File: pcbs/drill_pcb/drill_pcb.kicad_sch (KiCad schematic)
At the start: 78 parts, among them SW1 RPi reset, SW2 SW_Push, SW3 SW_Push, SW4 SW_Push, U1 PCA9306, U2 Pico, U3 L7805, U4 IFX007T, U5 IFX007T, U6 ACS712xLCTR-20A, U7 HT75xx-1-SOT89

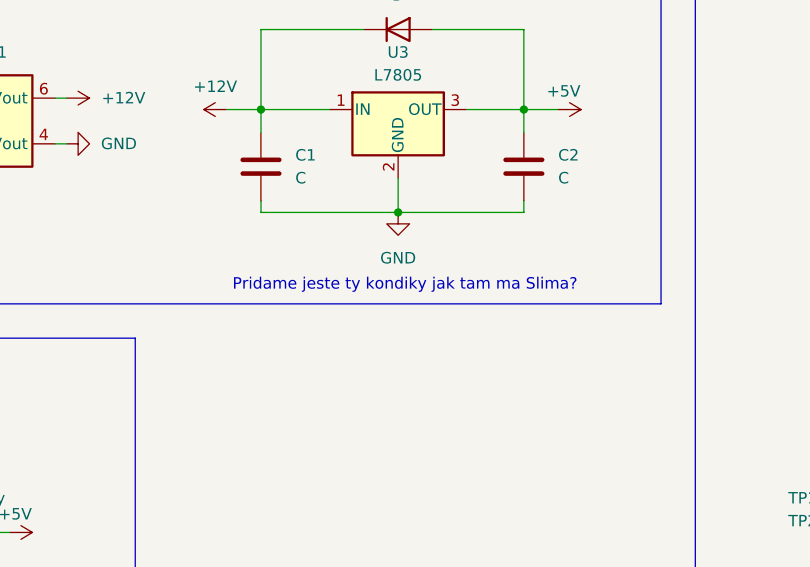
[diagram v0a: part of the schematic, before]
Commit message: delete comments
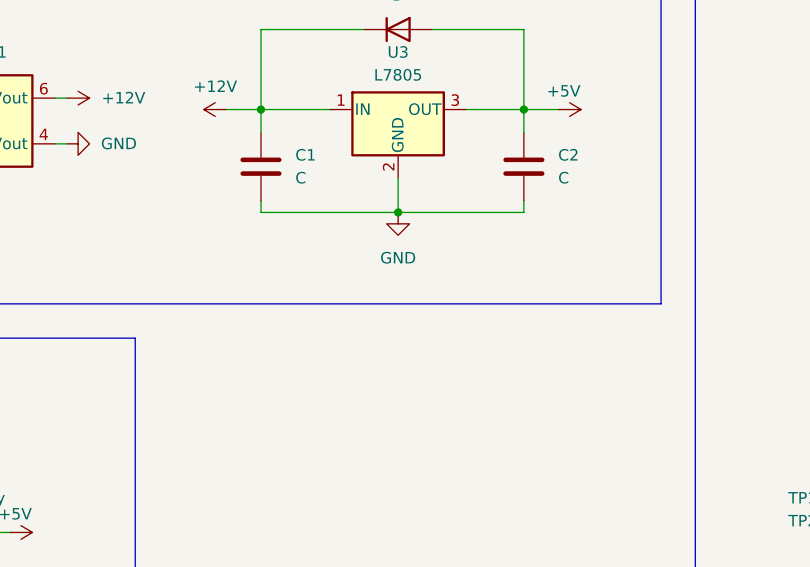
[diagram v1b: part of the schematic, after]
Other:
- note removed: "Pridame jeste ty kondiky jak tam ma Slima?"
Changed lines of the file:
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@@
-		)
-	)
-	(text "Pridame jeste ty kondiky jak tam ma Slima?"
-		(exclude_from_sim no)
-		(at 153.162 51.308 0)
-		(effects
-			(font
-				(size 1.27 1.27)
-			)
 		)
 	)

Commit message: pridany_pojezd
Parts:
- added A4: Arduino_Nano_v3.x, Module:Arduino_Nano, symbol MCU_Module:Arduino_Nano_v3.x
- added A5, A6: Driver_TMC2209, Module:Pololu_Breakout-16_15.2x20.3mm, symbol mujDriver:mujDriver2
- added C18, C21: 4μ7, Capacitor_THT:CP_Radial_D5.0mm_P2.50mm, symbol Device:C_Polarized
- added C19, C20: 100 nF, Capacitor_THT:C_Disc_D4.3mm_W1.9mm_P5.00mm, symbol Device:C
- added C22, C23: 100μ, Capacitor_THT:CP_Radial_D8.0mm_P3.50mm, symbol Device:C_Polarized
- added J1: 12V, Connector_AMASS:AMASS_XT60-M_1x02_P7.20mm_Vertical, symbol Connector:Screw_Terminal_01x02
- added J10: TOF_senzor, Connector_JST:JST_XH_B3B-XH-A_1x03_P2.50mm_Vertical, symbol Connector:Screw_Terminal_01x03
- added J11, J12, J5, J6: Screw_Terminal_01x03, Connector_JST:JST_XH_S3B-XH-A-1_1x03_P2.50mm_Horizontal, symbol Connector:Screw_Terminal_01x03
- added J2: Screw_Terminal_01x06, Connector_JST:JST_XH_B6B-XH-A_1x06_P2.50mm_Vertical, symbol Connector:Screw_Terminal_01x06
- added J3: I2C, Connector_JST:JST_XH_B2B-XH-A_1x02_P2.50mm_Vertical, symbol Connector:Screw_Terminal_01x02
- added J4: motor1, Connector_JST:JST_XH_B4B-XH-A_1x04_P2.50mm_Vertical, symbol Connector:Screw_Terminal_01x04
- added J7: Screw_Terminal_01x06, Connector_JST:JST_XH_S6B-XH-A-1_1x06_P2.50mm_Horizontal, symbol Connector:Screw_Terminal_01x06
- added J8: motor2, Connector_JST:JST_XH_B4B-XH-A_1x04_P2.50mm_Vertical, symbol Connector:Screw_Terminal_01x04
- added J9: 24V, kiCad:DEANS, symbol Connector:Screw_Terminal_01x02
- added R15: 1k, Resistor_SMD:R_1206_3216Metric, symbol Device:R
- added U8: LM7805_TO220, Package_TO_SOT_THT:TO-220-3_Vertical, symbol Regulator_Linear:LM7805_TO220
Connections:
- net +12V: now also C18.1, C19.1, J1.2 (Pin_2), U8.1 (VI)
- net +24V: now also A5.16 (VM), A6.16 (VM), C22.1, C23.1, J9.1 (Pin_1)
- net +5V: now also A4.27 (+5V), A5.10 (VDD), A6.10 (VDD), A6.2 (MS1), C20.1, C21.1, J10.1 (Pin_1), J2.4 (Pin_4), U8.3 (VO)
- net GND: now also A4.29 (GND), A5.15 (GND), A5.9 (GND), A6.15 (GND), A6.9 (GND), C18.2, C19.2, C20.2, C21.2, C22.2, C23.2, J1.1 (Pin_1), J10.3 (Pin_3), J2.3 (Pin_3), J9.2 (Pin_2), U8.2 (GND)
- new net: A4.5 (D2), J2.1 (Pin_1)
- new net: A4.20 (A1), J2.2 (Pin_2)
- new net: A4.19 (A0), J2.5 (Pin_5)
- new net: A4.6 (D3), J2.6 (Pin_6)
- new net: A4.23 (A4), J3.1 (Pin_1)
- new net: A4.24 (A5), J3.2 (Pin_2)
- new net: J11.2 (Pin_2), J12.3 (Pin_3), J5.2 (Pin_2), J6.1 (Pin_1), J7.4 (Pin_4)
- new net: J6.2 (Pin_2), J7.2 (Pin_2)
- new net: J11.1 (Pin_1), J12.1 (Pin_1), J5.1 (Pin_1), J6.3 (Pin_3), J7.3 (Pin_3)
- new net: A4.7 (D4), J10.2 (Pin_2)
- new net: A4.9 (D6), A5.1 (EN)
- new net: A5.11 (B2), J4.4 (Pin_4)
- new net: A5.12 (B1), J4.3 (Pin_3)
- new net: A5.13 (A1), J4.2 (Pin_2)
- new net: A5.14 (A2), J4.1 (Pin_1)
- new net: A4.14 (D11), A5.4 (RX), A6.4 (RX), R15.1
- new net: A4.12 (D9), A5.7 (STEP)
- new net: A4.8 (D5), A5.8 (DIR)
- new net: J5.3 (Pin_3), J7.1 (Pin_1)
- new net: J12.2 (Pin_2), J7.5 (Pin_5)
- new net: J11.3 (Pin_3), J7.6 (Pin_6)
- new net: A4.15 (D12), R15.2
- new net: A4.11 (D8), A6.1 (EN)
- new net: A6.11 (B2), J8.4 (Pin_4)
- new net: A6.12 (B1), J8.3 (Pin_3)
- new net: A6.13 (A1), J8.2 (Pin_2)
- new net: A6.14 (A2), J8.1 (Pin_1)
- new net: A4.13 (D10), A6.7 (STEP)
- new net: A4.10 (D7), A6.8 (DIR)
- no-connect marks 64 -> 84

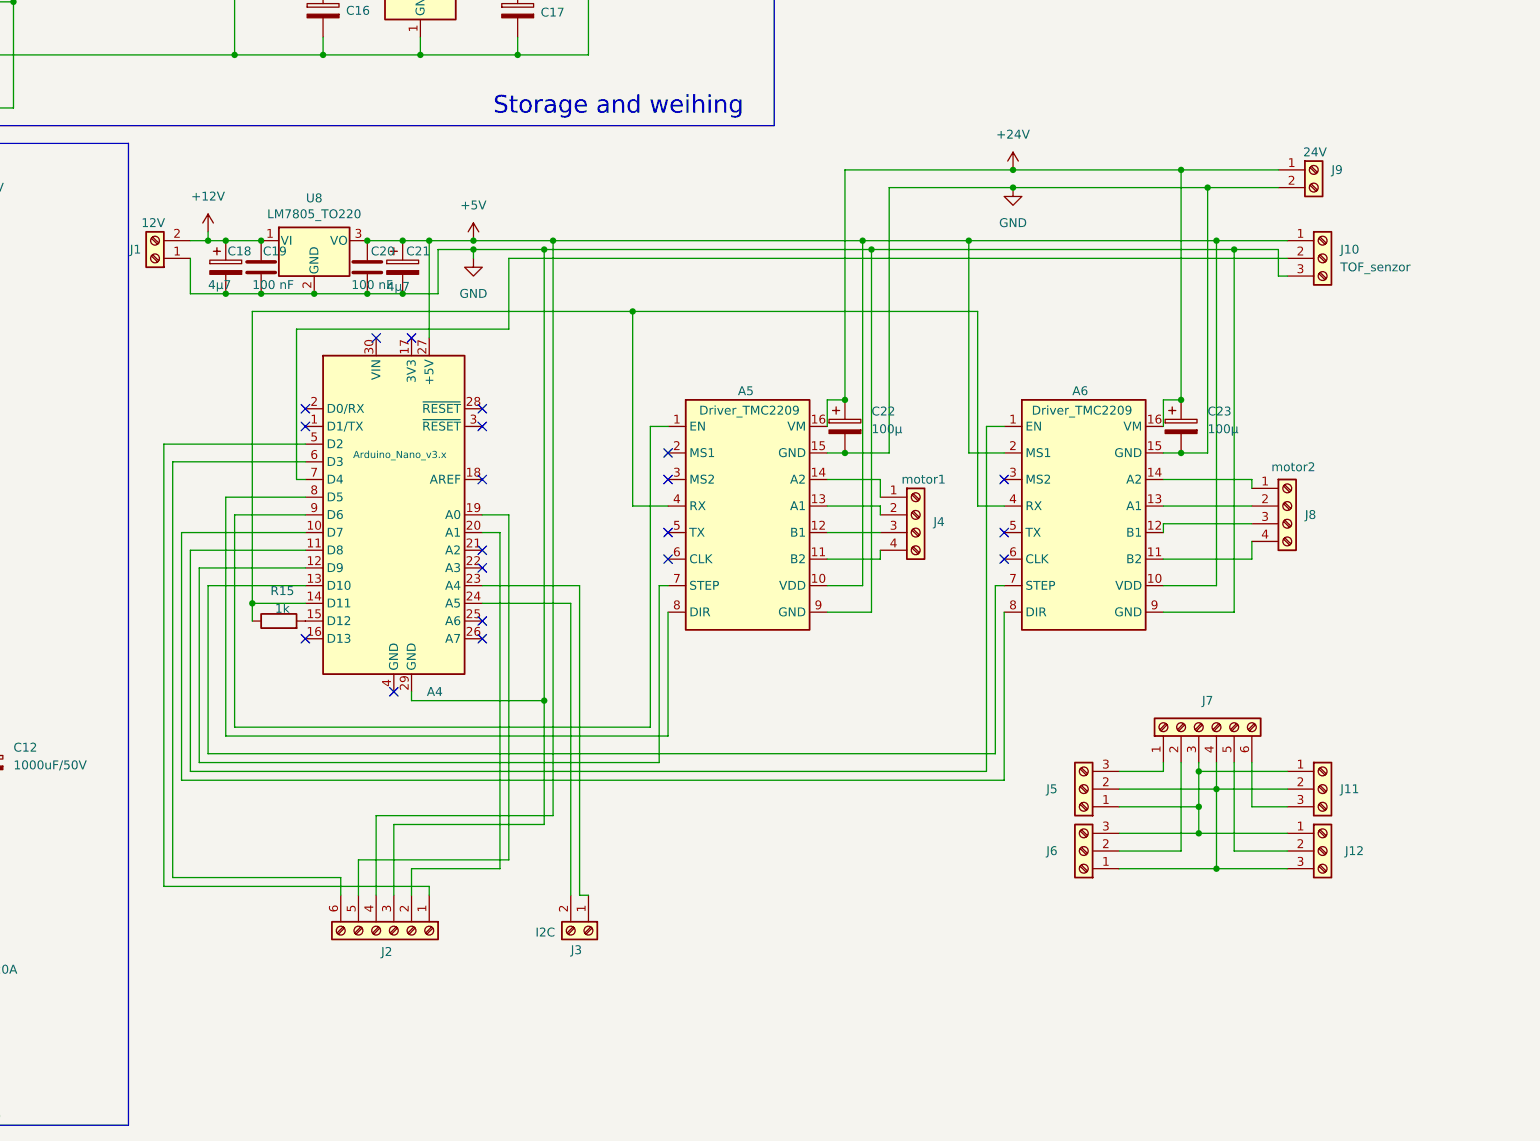
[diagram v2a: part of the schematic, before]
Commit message: add linear motor schematic
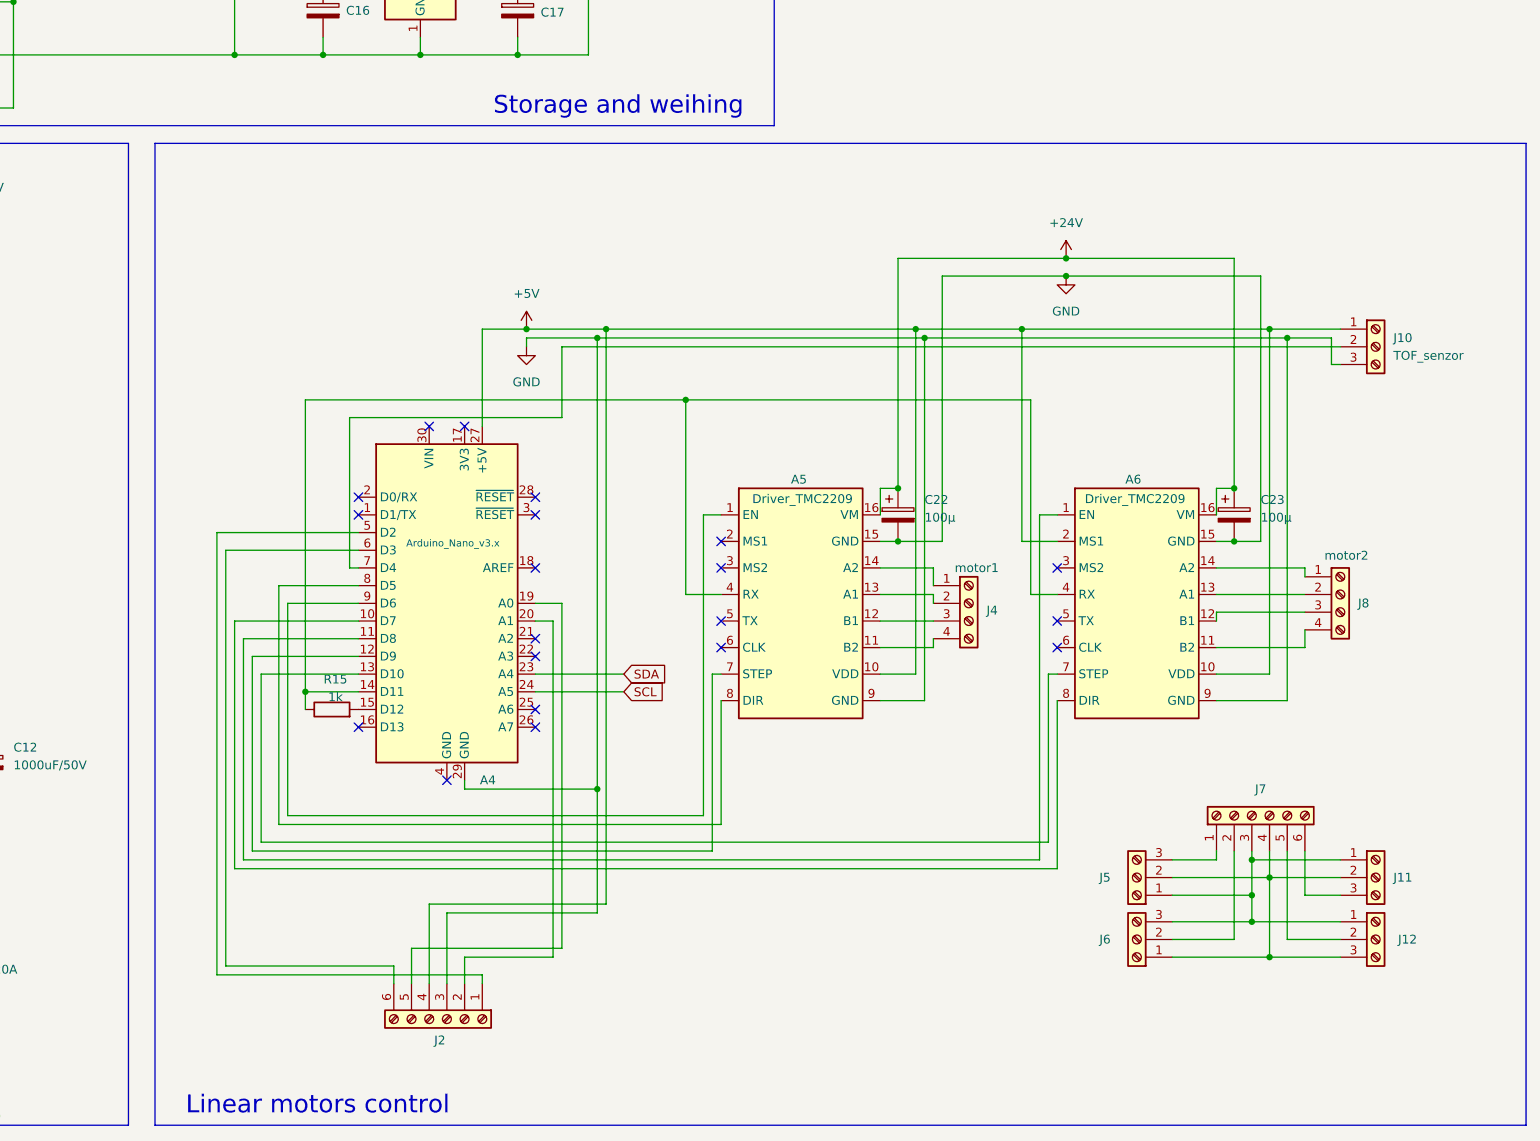
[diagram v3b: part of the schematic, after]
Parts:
- removed C18, C21: 4μ7, Capacitor_THT:CP_Radial_D5.0mm_P2.50mm, symbol Device:C_Polarized
- removed C19, C20: 100 nF, Capacitor_THT:C_Disc_D4.3mm_W1.9mm_P5.00mm, symbol Device:C
- removed J1: 12V, Connector_AMASS:AMASS_XT60-M_1x02_P7.20mm_Vertical, symbol Connector:Screw_Terminal_01x02
- removed J3: I2C, Connector_JST:JST_XH_B2B-XH-A_1x02_P2.50mm_Vertical, symbol Connector:Screw_Terminal_01x02
- removed J9: 24V, kiCad:DEANS, symbol Connector:Screw_Terminal_01x02
- removed U8: LM7805_TO220, Package_TO_SOT_THT:TO-220-3_Vertical, symbol Regulator_Linear:LM7805_TO220
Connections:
- net SCL: now also A4.24 (A5)
- net SDA: now also A4.23 (A4)
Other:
- note added: "Linear motors control"
- moved on the sheet: A4, A5, A6, C22, C23, J10, J11, J12, J2, J4, J5, J6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

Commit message: pcb update
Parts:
- A: renamed from 111; footprint hx711footp:HX711 -> drill_hx711footp:HX711
- A1, A2, A4: symbol MCU_Module:Arduino_Nano_v3.x -> drill_arduinoNanoEdit:arduinoNanoEdit
- renumbered Motor to Motor1, Tenzometry to Tenzometry1, hall_senzor to hall_senzor1
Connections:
- net +12V: no longer A1.30 (VIN)
- no-connect marks 84 -> 85
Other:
- note added: "Storage and weighing"
- note removed: "Storage and weihing"
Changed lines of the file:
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@@
 	)
 	(no_connect
+		(at 45.72 184.15)
+	)
+	(no_connect
 		(at 240.03 80.01)
 	)
@@
 	(wire
 		(pts
-			(xy 45.72 179.07) (xy 45.72 184.15)
-		)
-		(stroke
-			(width 0)
-			(type default)
-		)
-	)
-	(wire
-		(pts
 			(xy 419.1 248.92) (xy 419.1 242.57)
 		)
@@
 		)
 	)
-	(text "Storage and weihing"
+	(text "Storage and weighing"
 		(exclude_from_sim no)
 		(at 320.548 135.636 0)
@@
 	(symbol
 		(lib_id "power:+12V")
-		(at 45.72 179.07 0)
-		(unit 1)
-		(exclude_from_sim no)
-		(in_bom yes)
-		(on_board yes)
-		(dnp no)
-		(fields_autoplaced yes)
-		(property "Reference" "#PWR019"
-			(at 45.72 182.88 0)
-			(effects
-				(font
-					(size 1.27 1.27)
-				)
-				(hide yes)
-			)
-		)
-		(property "Value" "+12V"
-			(at 45.72 173.99 0)
-			(effects
-				(font
-					(size 1.27 1.27)
-				)
-			)
-		)
-		(property "Footprint" ""
-			(at 45.72 179.07 0)
-			(effects
-				(font
-					(size 1.27 1.27)
-				)
-				(hide yes)
-			)
-		)
-		(property "Datasheet" ""
-			(at 45.72 179.07 0)
-			(effects
-				(font
-					(size 1.27 1.27)
-				)
-				(hide yes)
-			)
-		)
-		(property "Description" "Power symbol creates a global label with name \"+12V\""
-			(at 45.72 179.07 0)
-			(effects
-				(font
-					(size 1.27 1.27)
-				)
-				(hide yes)
-			)
-		)
-		(pin "1"
-		)
-		(instances
-			(project "drill_pcb"
-				(path "/bebf97b1-2f7f-4d03-a427-fe976f4b2313"
-					(reference "#PWR019")
-					(unit 1)
-				)
-			)
-		)
-	)
-	(symbol
-		(lib_id "power:+12V")
 		(at 115.57 30.48 270)
 		(unit 1)
@@
 		(on_board yes)
 		(dnp no)
-		(property "Reference" "Tenzometry"
+		(property "Reference" "Tenzometry1"
 			(at 330.2 86.3599 0)
 			(effects
@@
 			(project "drill_pcb"
 				(path "/bebf97b1-2f7f-4d03-a427-fe976f4b2313"
-					(reference "Tenzometry")
+					(reference "Tenzometry1")
 					(unit 1)
 				)
@@
 	)
 	(symbol
-		(lib_id "MCU_Module:Arduino_Nano_v3.x")
+		(lib_id "drill_arduinoNanoEdit:arduinoNanoEdit")
 		(at 48.26 209.55 0)
 		(unit 1)
@@
 		(on_board yes)
 		(dnp no)
-		(property "Reference" "111"
+		(property "Reference" "A"
 			(at 307.34 96.52 0)
 			(effects
@@
 			)
 		)
-		(property "Footprint" "hx711footp:HX711"
+		(property "Footprint" "drill_hx711footp:HX711"
 			(at 307.34 96.52 0)
 			(effects
@@
 			(project "drill_pcb"
 				(path "/bebf97b1-2f7f-4d03-a427-fe976f4b2313"
-					(reference "111")
+					(reference "A")
 					(unit 1)
 				)
@@
 		(dnp no)
 		(fields_autoplaced yes)
-		(property "Reference" "hall_senzor"
+		(property "Reference" "hall_senzor1"
 			(at 330.2 114.2999 0)
 			(effects
@@
 			(project "drill_pcb"
 				(path "/bebf97b1-2f7f-4d03-a427-fe976f4b2313"
-					(reference "hall_senzor")
+					(reference "hall_senzor1")
 					(unit 1)
 				)
@@
 		(dnp no)
 		(fields_autoplaced yes)
-		(property "Reference" "Motor"
+		(property "Reference" "Motor1"
 			(at 330.2 45.7199 0)
 			(effects
@@
 			(project "drill_pcb"
 				(path "/bebf97b1-2f7f-4d03-a427-fe976f4b2313"
-					(reference "Motor")
+					(reference "Motor1")
 					(unit 1)
 				)
@@
 	)
 	(symbol
-		(lib_id "MCU_Module:Arduino_Nano_v3.x")
+		(lib_id "drill_arduinoNanoEdit:arduinoNanoEdit")
 		(at 227.33 62.23 0)
 		(unit 1)
@@
 	)
 	(symbol
-		(lib_id "MCU_Module:Arduino_Nano_v3.x")
+		(lib_id "drill_arduinoNanoEdit:arduinoNanoEdit")
 		(at 295.91 207.01 0)
 		(unit 1)

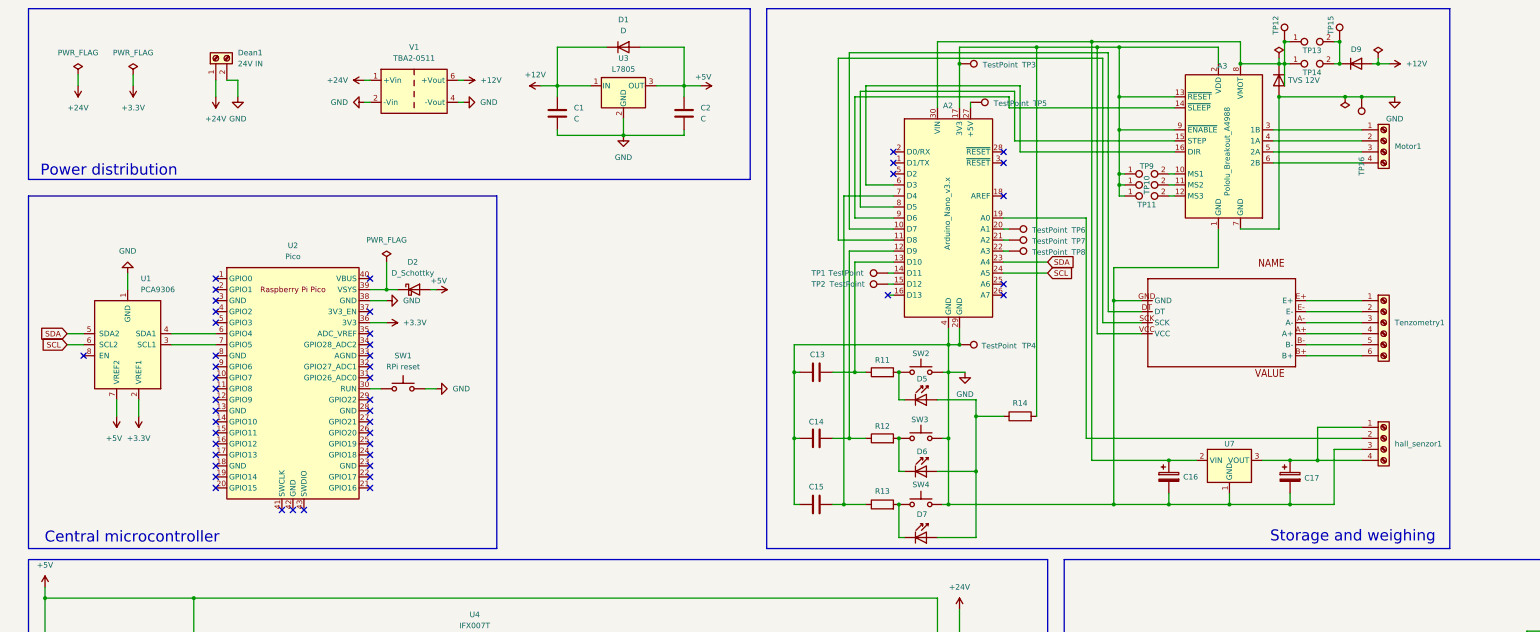
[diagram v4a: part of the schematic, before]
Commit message: PCB power distribution update
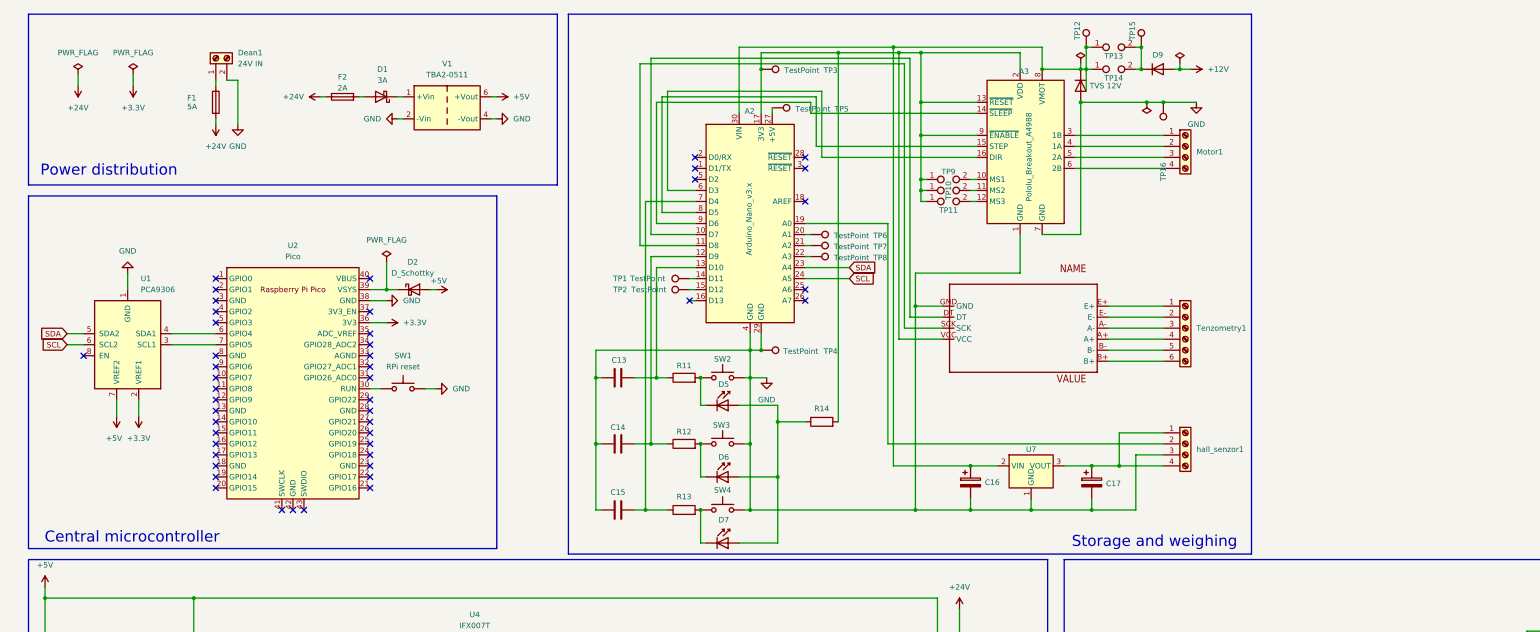
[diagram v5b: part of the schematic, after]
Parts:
- removed C1, C2: C, Capacitor_SMD:C_1206_3216Metric_Pad1.33x1.80mm_HandSolder, symbol Device:C
- removed D1: D, Diode_THT:D_DO-41_SOD81_P7.62mm_Horizontal, symbol Device:D
- removed U3: L7805, Package_TO_SOT_THT:TO-220-3_Vertical, symbol Regulator_Linear:L7805
- added D1: 3A, Diode_SMD:D_SMC_Handsoldering, symbol Device:D_Schottky
- added F1: 5A, Fuse:Fuse_Blade_ATO_directSolder, symbol Device:Fuse
- added F2: 2A, Fuse:Fuse_Blade_ATO_directSolder, symbol Device:Fuse
- renumbered A to A7
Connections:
- net +12V: no longer V1.6 (+Vout)
- net +24V: now also F1.2, F2.1; no longer Dean1.1 (Pin_1), V1.1 (+Vin)
- net +5V: now also V1.6 (+Vout)
- new net: Dean1.1 (Pin_1), F1.1
- new net: D1.1 (K), V1.1 (+Vin)
- new net: D1.2 (A), F2.2
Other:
- moved on the sheet: A2, A3, C13, C14, C15, C16, C17, D5, D6, D7, D9, Motor1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
